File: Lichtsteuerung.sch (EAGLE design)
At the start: 136 parts, among them IC1 74HC595D, IC10 TSR_1-2450, IC11 MEGA64-A, IC12 75176AD, IC13 DS1307SO8, IC2 74HC595D, IC3 74HC595D, IC4 74HC595D, IC5 75176AD, IC6 MEGA8-AI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

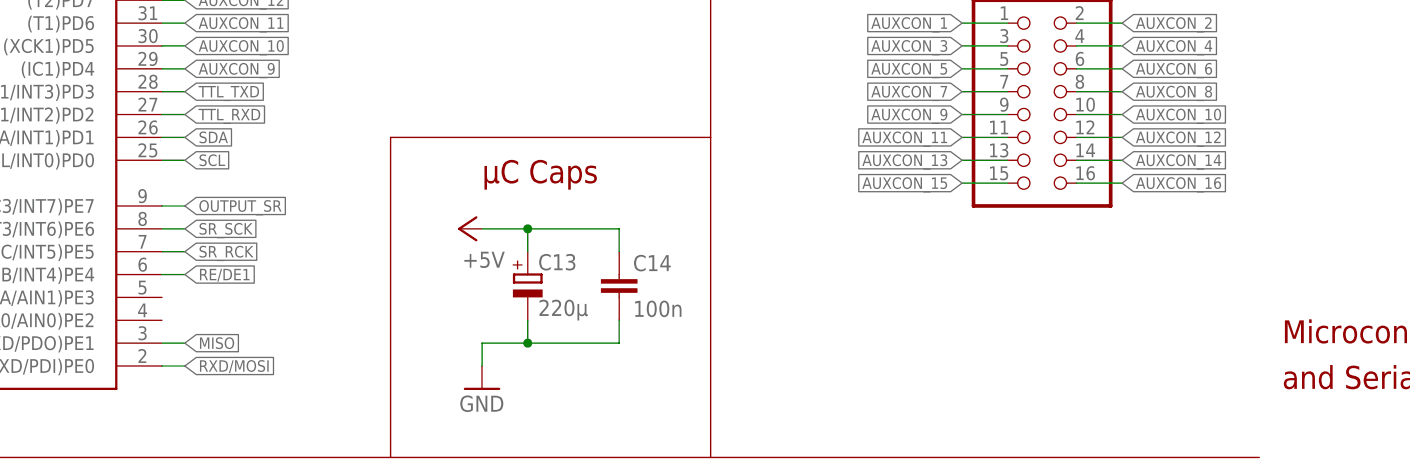
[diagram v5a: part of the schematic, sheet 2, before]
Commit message: Added another aux connector to supply SDA, SCL, +5V and GND
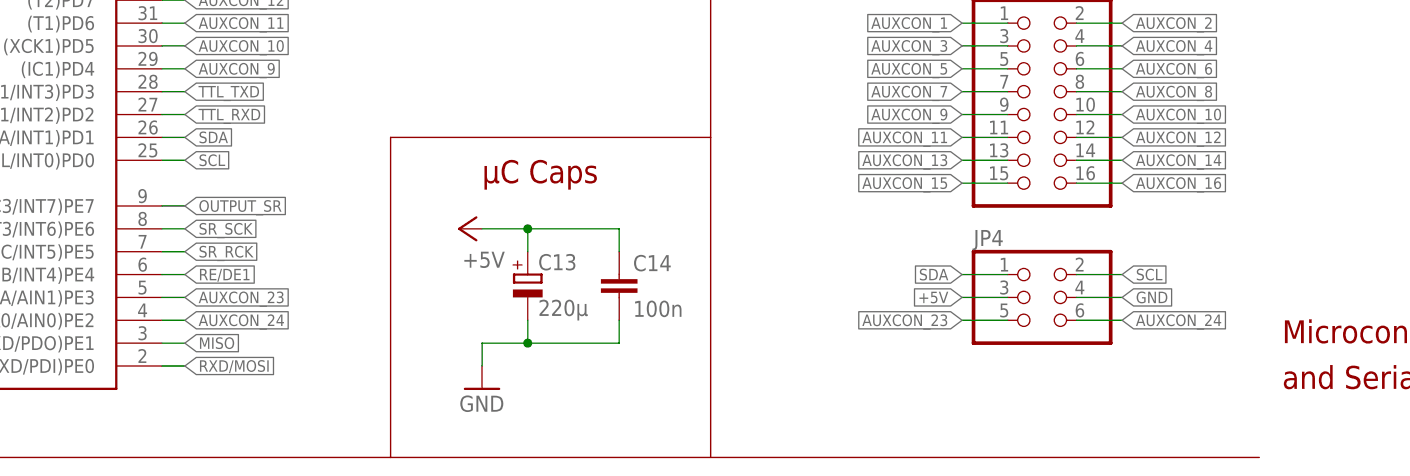
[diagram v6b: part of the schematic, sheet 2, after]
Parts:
- added JP4: (no value), pinhead:PINHD-2X3
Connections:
- new net AUXCON_23: IC11.(OC3A/AIN1)PE3, JP4.5
- new net AUXCON_24: IC11.(XCK0/AIN0)PE2, JP4.6
- net +5V: now also JP4.3
- net GND: now also JP4.4
- net SCL: now also JP4.2
- net SDA: now also JP4.1
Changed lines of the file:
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@@
 <part name="F5" library="ptc-littlefuse" deviceset="1812L" device="" value="500mA"/>
 <part name="C21" library="resistor" deviceset="C-EU" device="C0805" value="100n"/>
+<part name="JP4" library="pinhead" deviceset="PINHD-2X3" device=""/>
 </parts>
 <sheets>
@@
 </instance>
 <instance part="C21" gate="G$1" x="106.68" y="180.34"/>
+<instance part="JP4" gate="A" x="261.62" y="25.4"/>
 </instances>
 <busses>
@@
 <pinref part="X7" gate="G$1" pin="P1"/>
 </segment>
+<segment>
+<pinref part="JP4" gate="A" pin="2"/>
+<wire x1="266.7" y1="27.94" x2="271.78" y2="27.94" width="0.1524" layer="91"/>
+<label x="271.78" y="27.94" size="1.27" layer="95" xref="yes"/>
+</segment>
 </net>
 <net name="SDA" class="0">
@@
 <pinref part="X7" gate="G$1" pin="P2"/>
 </segment>
+<segment>
+<pinref part="JP4" gate="A" pin="1"/>
+<wire x1="259.08" y1="27.94" x2="254" y2="27.94" width="0.1524" layer="91"/>
+<label x="254" y="27.94" size="1.27" layer="95" rot="R180" xref="yes"/>
+</segment>
 </net>
 <net name="+5V" class="0">
@@
 <pinref part="IC6" gate="G$1" pin="AVCC"/>
 </segment>
+<segment>
+<pinref part="JP4" gate="A" pin="3"/>
+<wire x1="259.08" y1="25.4" x2="254" y2="25.4" width="0.1524" layer="91"/>
+<label x="254" y="25.4" size="1.27" layer="95" rot="R180" xref="yes"/>
+</segment>
 </net>
 <net name="N$42" class="0">
@@
 <pinref part="X6" gate="G$1" pin="P1"/>
 </segment>
+<segment>
+<pinref part="JP4" gate="A" pin="4"/>
+<wire x1="266.7" y1="25.4" x2="271.78" y2="25.4" width="0.1524" layer="91"/>
+<label x="271.78" y="25.4" size="1.27" layer="95" xref="yes"/>
+</segment>
 </net>
 <net name="+24V" class="1">
@@
 </segment>
 </net>
+<net name="AUXCON_23" class="0">
+<segment>
+<pinref part="IC11" gate="G$1" pin="(OC3A/AIN1)PE3"/>
+<wire x1="165.1" y1="25.4" x2="167.64" y2="25.4" width="0.1524" layer="91"/>
+<label x="167.64" y="25.4" size="1.27" layer="95" xref="yes"/>
+</segment>
+<segment>
+<pinref part="JP4" gate="A" pin="5"/>
+<wire x1="259.08" y1="22.86" x2="256.54" y2="22.86" width="0.1524" layer="91"/>
+<wire x1="256.54" y1="22.86" x2="254" y2="22.86" width="0.1524" layer="91"/>
+<label x="254" y="22.86" size="1.27" layer="95" rot="R180" xref="yes"/>
+</segment>
+</net>
+<net name="AUXCON_24" class="0">
+<segment>
+<pinref part="IC11" gate="G$1" pin="(XCK0/AIN0)PE2"/>
+<wire x1="165.1" y1="22.86" x2="167.64" y2="22.86" width="0.1524" layer="91"/>
+<label x="167.64" y="22.86" size="1.27" layer="95" xref="yes"/>
+</segment>
+<segment>
+<pinref part="JP4" gate="A" pin="6"/>
+<wire x1="266.7" y1="22.86" x2="271.78" y2="22.86" width="0.1524" layer="91"/>
+<label x="271.78" y="22.86" size="1.27" layer="95" xref="yes"/>
+</segment>
+</net>

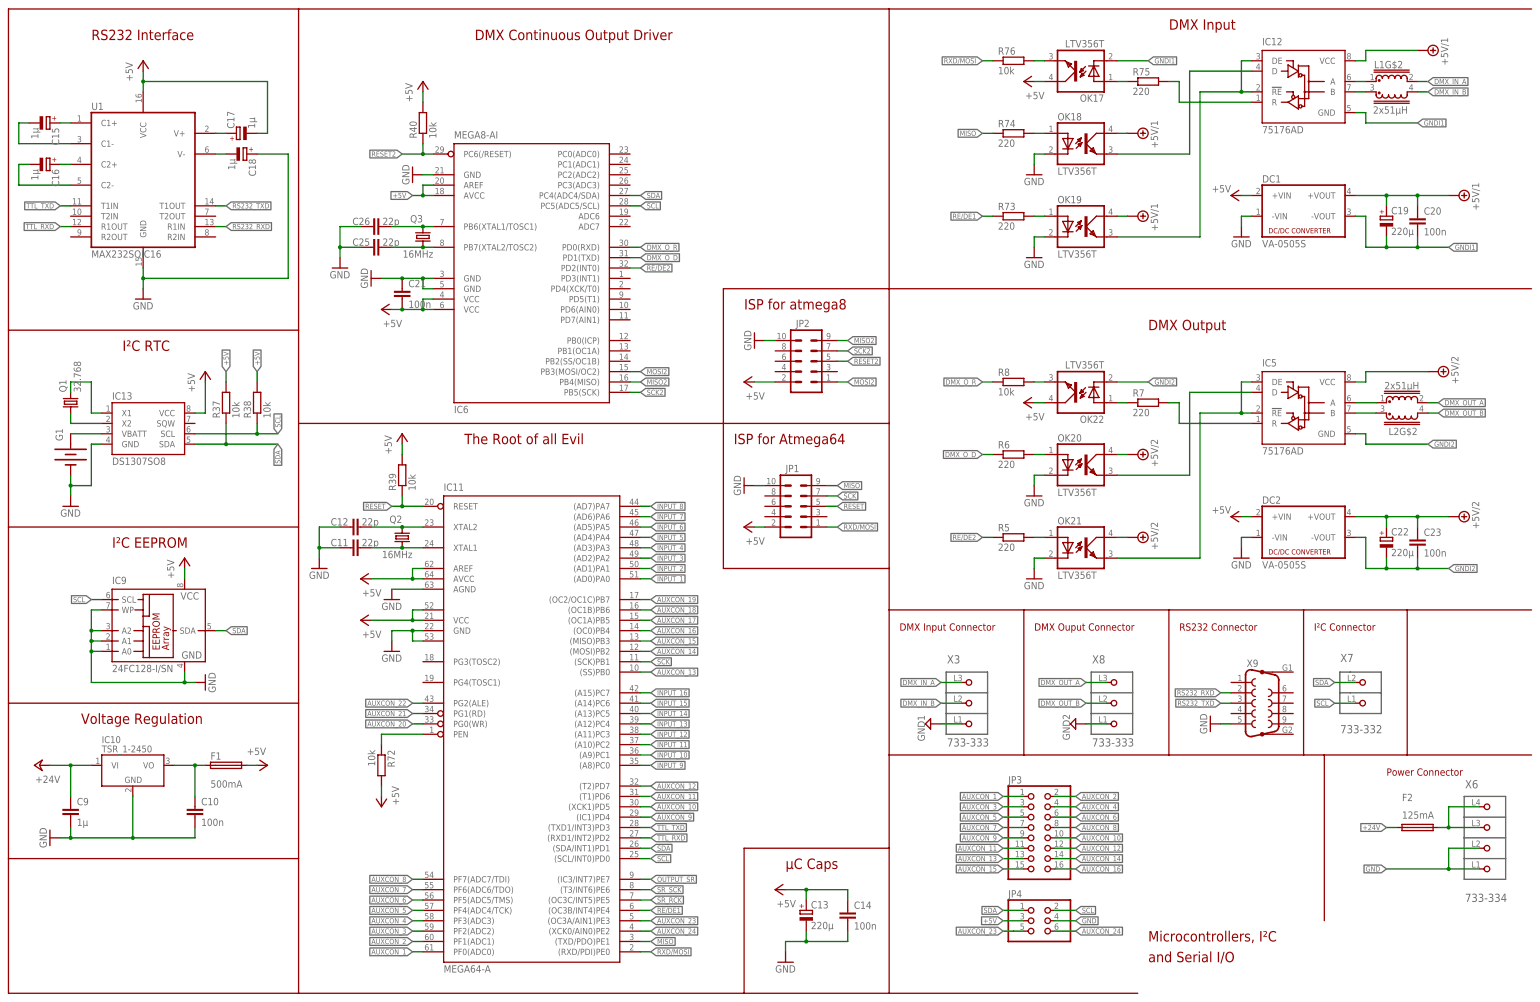
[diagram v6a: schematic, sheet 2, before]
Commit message: - Added GND for I²C connector - Added LEDs for power indication - Added output enable for shift registers - Moved pin headers to make room for cable - Added pullup/pulldown resistors and SMD jumpers to configure DMX line termination
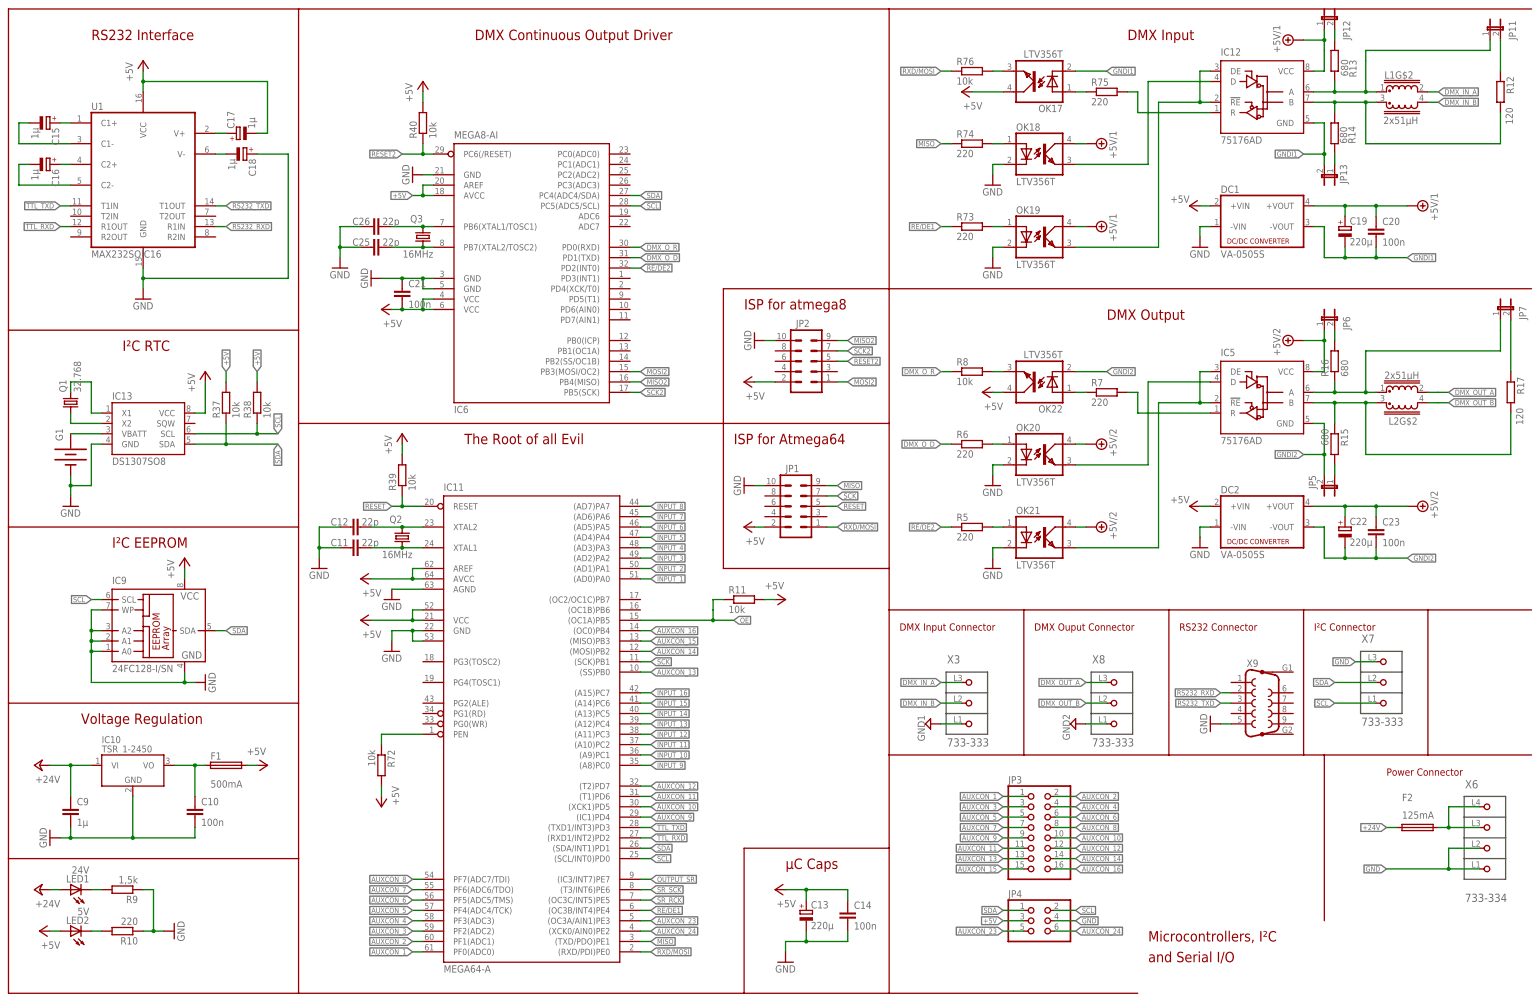
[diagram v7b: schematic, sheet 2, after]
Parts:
- added JP11, JP12, JP13, JP5, JP6, JP7: (no value), SparkFun:JUMPER-2SMD-NC
- added LED1: 24V, led:LEDCHIP-LED0805
- added LED2: 5V, led:LEDCHIP-LED0805
- added R10: 220, rcl:R-EU_R0805
- added R11: 10k, resistor:R-EU_R0805
- added R12, R17: 120, rcl:R-EU_R0805
- added R13, R14, R15, R16: 680, rcl:R-EU_R0805
- added R9: 1,5k, rcl:R-EU_R0805
- X7: value 733-332 -> 733-333; device con-wago_2.5mm:733-332 -> con-wago_2.5mm:733-333
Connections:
- removed net AUXCON_17: IC11.(OC1A)PB5
- removed net AUXCON_18: IC11.(OC1B)PB6
- removed net AUXCON_19: IC11.(OC2/OC1C)PB7
- removed net AUXCON_20: IC11.PG0(WR)
- removed net AUXCON_21: IC11.PG1(RD)
- removed net AUXCON_22: IC11.PG2(ALE)
- removed net N$73: IC12.B, L1G$2.1
- removed net N$79: IC5.B, L2G$2.1
- new net N$101: IC12.B, L1G$2.1, R12.2, R14.2
- new net N$80: LED1.C, R9.2
- new net N$82: LED2.C, R10.2
- new net N$85: JP12.2, R13.2
- new net N$86: JP13.1, R14.1
- new net N$88: IC5.B, L2G$2.1, R15.1, R17.2
- new net N$89: JP11.2, R12.1
- new net N$91: JP5.1, R15.2
- new net N$92: JP7.2, R17.1
- new net N$94: JP6.2, R16.2
- new net OE: IC11.(OC1A)PB5, IC1A.G, IC2A.G, IC3A.G, IC4A.G, R11.1
- net +24V: now also LED1.A
- net +5V: now also LED2.A, R11.2
- net GND: now also R10.1, R9.1, X7.P3; no longer IC1A.G, IC2A.G, IC3A.G, IC4A.G
- net GNDI1: now also JP13.2
- net GNDI2: now also JP5.2
- net N$53: now also JP11.1, R13.1
- net N$77: now also JP7.1, R16.1
- net VCCIO1: now also JP12.1
- net VCCIO2: now also JP6.1
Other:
- moved on the sheet: C19, C20, C22, C23, DC1, DC2, IC12, IC5, L1G$2, L2G$2, OK17, OK18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

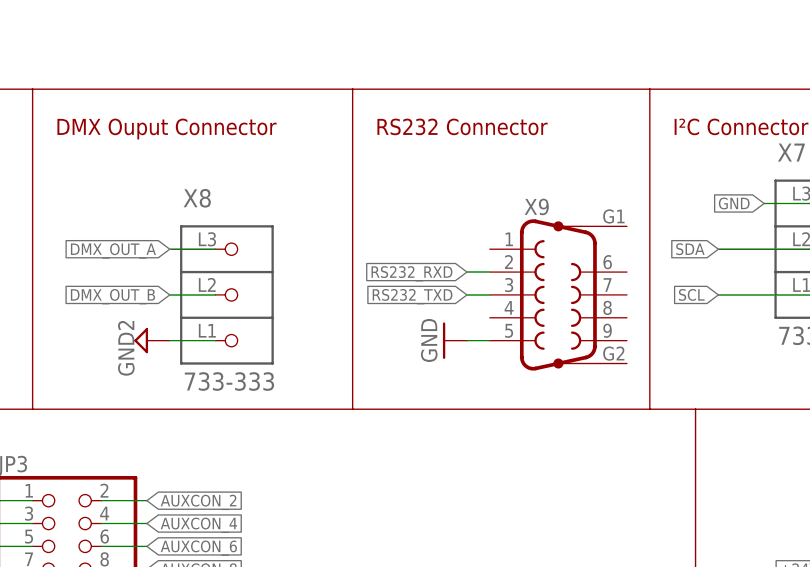
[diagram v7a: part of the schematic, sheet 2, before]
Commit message: Swapped RXD and TXD, because this is a DCE, not a DTE. In plain words: You can simply connect any USB-RS232 connector to the port now, instead of using a null modem cable with crossed RXD/TXD pairs.
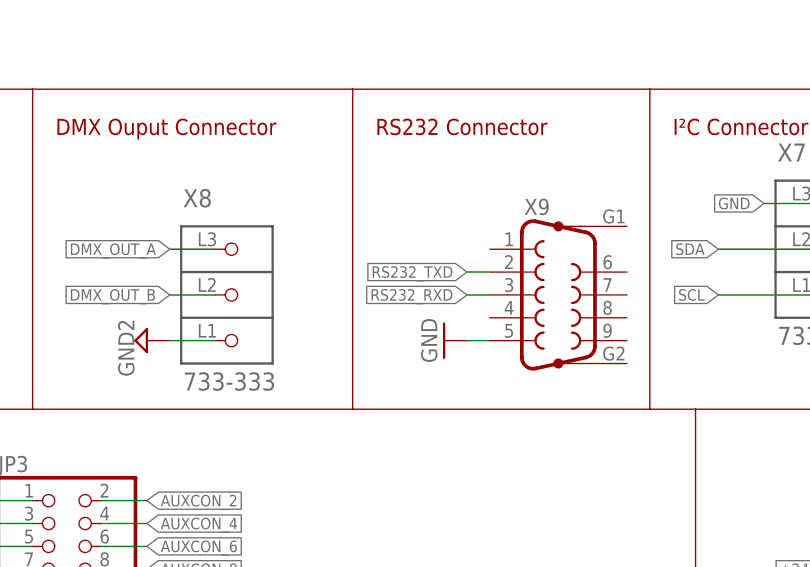
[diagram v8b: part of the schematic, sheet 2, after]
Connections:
- net RS232_RXD: now also X9.3; no longer X9.2
- net RS232_TXD: now also X9.2; no longer X9.3
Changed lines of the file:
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@@
 </segment>
 <segment>
-<wire x1="309.88" y1="81.28" x2="307.34" y2="81.28" width="0.1524" layer="91"/>
-<label x="307.34" y="81.28" size="1.27" layer="95" rot="R180" xref="yes"/>
-<pinref part="X9" gate="G$1" pin="2"/>
+<wire x1="309.88" y1="78.74" x2="307.34" y2="78.74" width="0.1524" layer="91"/>
+<label x="307.34" y="78.74" size="1.27" layer="95" rot="R180" xref="yes"/>
+<pinref part="X9" gate="G$1" pin="3"/>
 </segment>
 </net>
@@
 </segment>
 <segment>
-<wire x1="309.88" y1="78.74" x2="307.34" y2="78.74" width="0.1524" layer="91"/>
-<label x="307.34" y="78.74" size="1.27" layer="95" rot="R180" xref="yes"/>
-<pinref part="X9" gate="G$1" pin="3"/>
+<wire x1="309.88" y1="81.28" x2="307.34" y2="81.28" width="0.1524" layer="91"/>
+<label x="307.34" y="81.28" size="1.27" layer="95" rot="R180" xref="yes"/>
+<pinref part="X9" gate="G$1" pin="2"/>
 </segment>
 </net>
